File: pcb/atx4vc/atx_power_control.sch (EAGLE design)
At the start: 60 parts, among them IC2 REG1117, IC3 STM32F042F4, IC4 MY_7905DT, J1 ATX24RH, SW1 324_SW, SW2 324_SW, SW3 324_SW, SW4 324_SW, SW5 324_SW, SW6 324_SW, SW7 324_SW, U1 USBC_16P, U2 USBC_16P

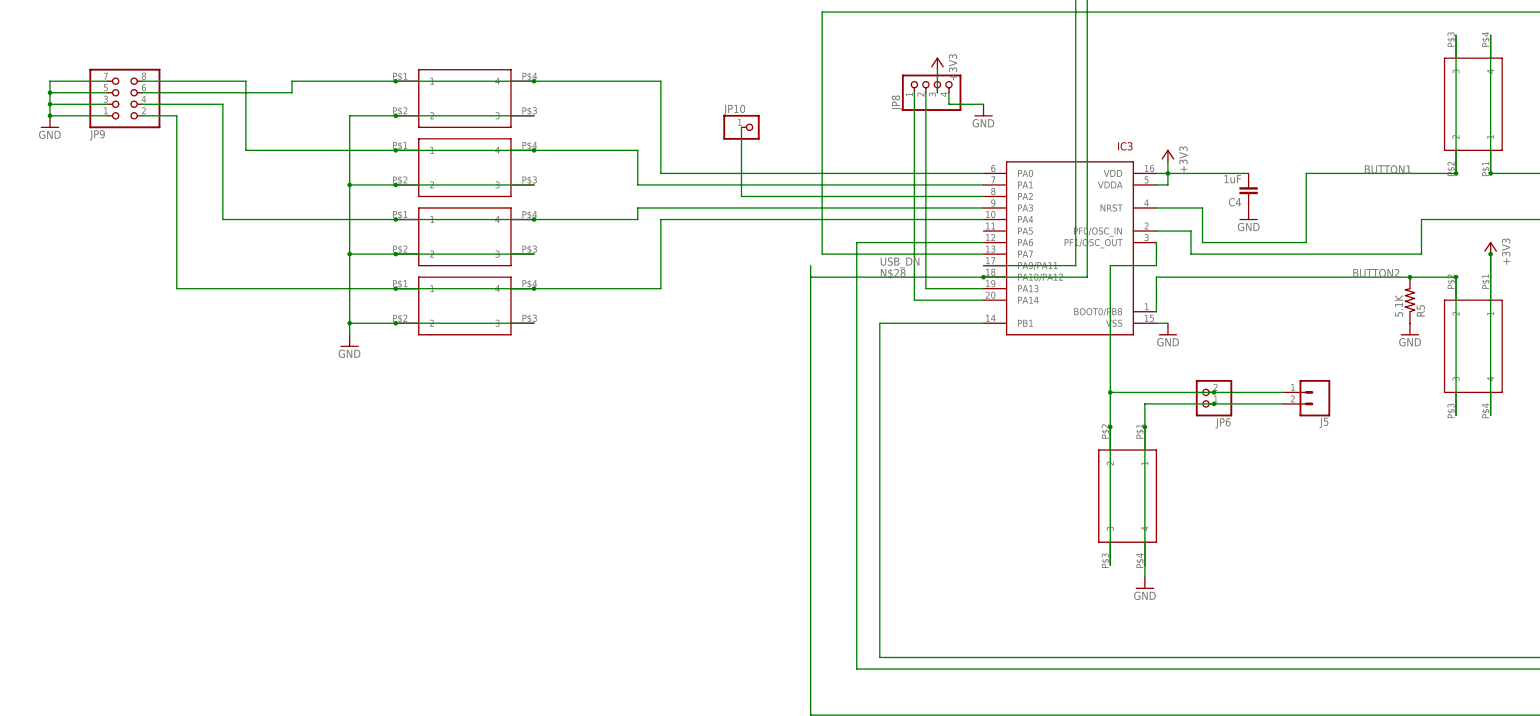
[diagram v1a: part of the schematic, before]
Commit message: added UART RX header, brightness button shared with DFU button
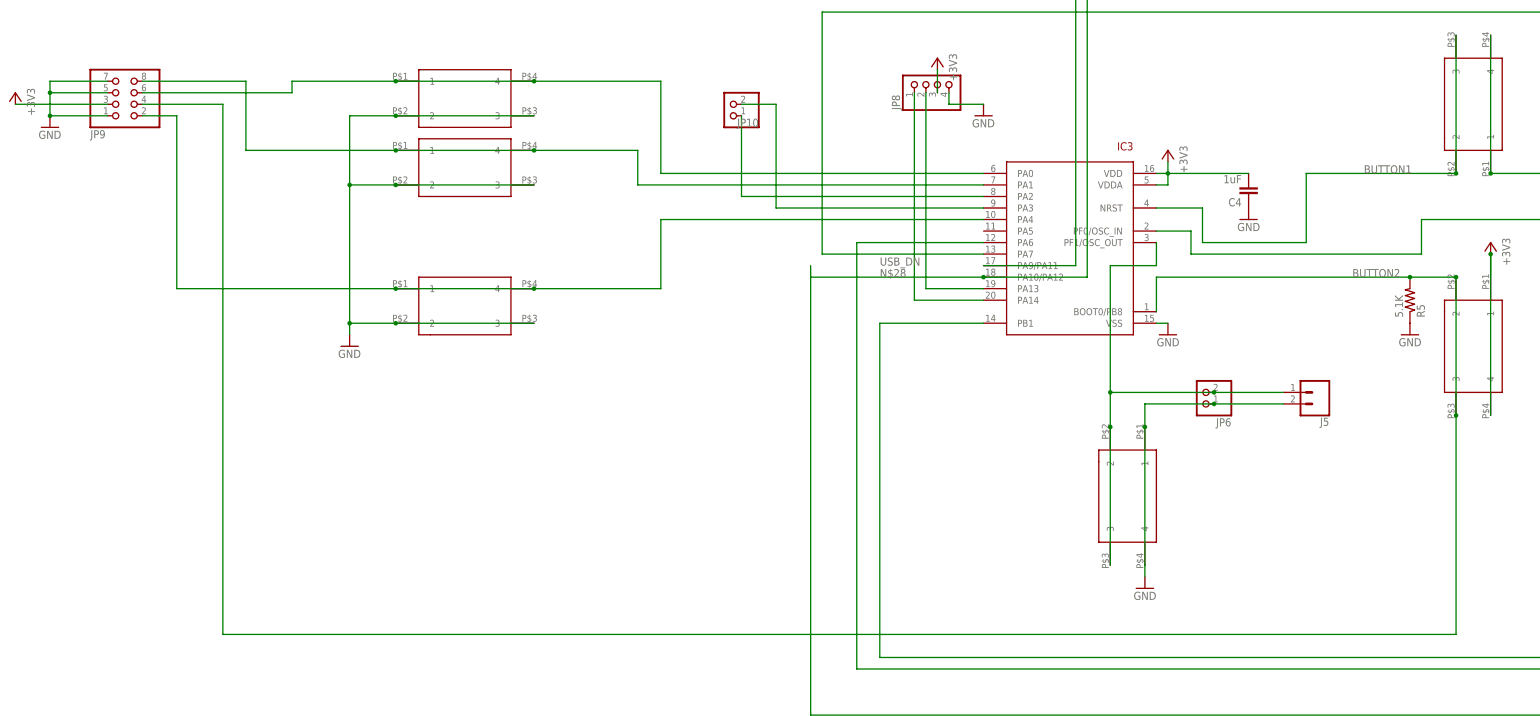
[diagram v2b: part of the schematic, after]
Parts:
- removed SW6: 324_SW, 3pos_slide_switch_centered:324_SW
- JP10: device adafruit_changed:PINHD-1X1 -> pinhead:PINHD-1X2
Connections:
- removed net N$30: IC3.PA3, JP9.4, SW6.1, SW6.4
- new net N$12: IC3.PA3, JP10.2
- net +3V3: now also JP9.3
- net BUTTON2: now also JP9.4
- net GND: no longer JP9.3, SW6.2, SW6.3
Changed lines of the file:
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@@
 <part name="J8" library="atx_power_control" deviceset="CONN_02" device="3.5MM"/>
 <part name="SW5" library="3pos_slide_switch_centered" deviceset="324_SW" device="" value="324_SW"/>
-<part name="SW6" library="3pos_slide_switch_centered" deviceset="324_SW" device="" value="324_SW"/>
 <part name="SW7" library="3pos_slide_switch_centered" deviceset="324_SW" device="" value="324_SW"/>
 <part name="GND30" library="backplane" deviceset="GND" device=""/>
 <part name="JP9" library="pinhead" library_urn="urn:adsk.eagle:library:325" deviceset="PINHD-2X4" device="" package3d_urn="urn:adsk.eagle:package:22461/2"/>
-<part name="JP10" library="adafruit_changed" deviceset="PINHD-1X1" device=""/>
+<part name="JP10" library="pinhead" library_urn="urn:adsk.eagle:library:325" deviceset="PINHD-1X2" device="" package3d_urn="urn:adsk.eagle:package:22435/2"/>
 <part name="U1" library="my_usbc_16p" deviceset="USBC_16P" device=""/>
 <part name="GND31" library="supply1" deviceset="GND" device=""/>
 <part name="R12" library="joyAnalog" deviceset="RESISTOR" device="0805-RES" value="5.1K"/>
 <part name="R13" library="joyAnalog" deviceset="RESISTOR" device="0805-RES" value="5.1K"/>
+<part name="+3V3" library="supply1" library_urn="urn:adsk.eagle:library:371" deviceset="+3V3" device=""/>
 </parts>
 <sheets>
@@
 </instance>
 <instance part="SW5" gate="G$1" x="-132.08" y="43.18" smashed="yes" rot="MR180"/>
-<instance part="SW6" gate="G$1" x="-132.08" y="27.94" smashed="yes" rot="MR180"/>
 <instance part="SW7" gate="G$1" x="-132.08" y="12.7" smashed="yes" rot="MR180"/>
 <instance part="GND30" gate="1" x="-223.52" y="50.8" smashed="yes">
@@
 <attribute name="VALUE" x="-214.63" y="66.04" size="1.778" layer="96" rot="MR180"/>
 </instance>
-<instance part="JP10" gate="G$1" x="-68.58" y="50.8" smashed="yes">
-<attribute name="NAME" x="-74.93" y="53.975" size="1.778" layer="95"/>
-<attribute name="VALUE" x="-74.93" y="45.72" size="1.778" layer="96"/>
+<instance part="JP10" gate="G$1" x="-73.66" y="55.88" smashed="yes" rot="R180">
+<attribute name="NAME" x="-67.31" y="52.705" size="1.778" layer="95" rot="R180"/>
+<attribute name="VALUE" x="-67.31" y="60.96" size="1.778" layer="96" rot="R180"/>
 </instance>
 <instance part="U1" gate="G$1" x="279.4" y="111.76" smashed="yes" rot="MR0"/>
@@
 <attribute name="NAME" x="250.19" y="128.4986" size="1.778" layer="95" rot="MR0"/>
 <attribute name="VALUE" x="250.19" y="123.698" size="1.778" layer="96" rot="MR0"/>
+</instance>
+<instance part="+3V3" gate="G$1" x="-231.14" y="58.42" smashed="yes" rot="MR0">
+<attribute name="VALUE" x="-228.6" y="53.34" size="1.778" layer="96" rot="MR90"/>
 </instance>
 </instances>
@@
 <pinref part="SW5" gate="G$1" pin="3"/>
 <pinref part="SW5" gate="G$1" pin="2"/>
-<wire x1="-157.48" y1="38.1" x2="-157.48" y2="22.86" width="0.1524" layer="91"/>
-<wire x1="-157.48" y1="22.86" x2="-157.48" y2="7.62" width="0.1524" layer="91"/>
+<wire x1="-157.48" y1="38.1" x2="-157.48" y2="7.62" width="0.1524" layer="91"/>
 <wire x1="-157.48" y1="7.62" x2="-157.48" y2="5.08" width="0.1524" layer="91"/>
 <wire x1="-116.84" y1="38.1" x2="-147.32" y2="38.1" width="0.1524" layer="91"/>
@@
 <junction x="-147.32" y="38.1"/>
 <junction x="-157.48" y="38.1"/>
-<pinref part="SW6" gate="G$1" pin="3"/>
-<pinref part="SW6" gate="G$1" pin="2"/>
-<wire x1="-116.84" y1="22.86" x2="-147.32" y2="22.86" width="0.1524" layer="91"/>
-<wire x1="-147.32" y1="22.86" x2="-157.48" y2="22.86" width="0.1524" layer="91"/>
-<junction x="-147.32" y="22.86"/>
-<junction x="-157.48" y="22.86"/>
 <pinref part="SW7" gate="G$1" pin="3"/>
 <pinref part="SW7" gate="G$1" pin="2"/>
@@
 <wire x1="-210.82" y1="60.96" x2="-223.52" y2="60.96" width="0.1524" layer="91"/>
 <wire x1="-223.52" y1="60.96" x2="-223.52" y2="58.42" width="0.1524" layer="91"/>
-<wire x1="-223.52" y1="58.42" x2="-223.52" y2="55.88" width="0.1524" layer="91"/>
-<wire x1="-223.52" y1="55.88" x2="-223.52" y2="53.34" width="0.1524" layer="91"/>
+<wire x1="-223.52" y1="58.42" x2="-223.52" y2="53.34" width="0.1524" layer="91"/>
 <wire x1="-210.82" y1="58.42" x2="-223.52" y2="58.42" width="0.1524" layer="91"/>
 <junction x="-223.52" y="58.42"/>
-<wire x1="-210.82" y1="55.88" x2="-223.52" y2="55.88" width="0.1524" layer="91"/>
-<junction x="-223.52" y="55.88"/>
 <wire x1="-210.82" y1="53.34" x2="-223.52" y2="53.34" width="0.1524" layer="91"/>
 <junction x="-223.52" y="53.34"/>
 <pinref part="JP9" gate="A" pin="1"/>
-<pinref part="JP9" gate="A" pin="3"/>
 <pinref part="JP9" gate="A" pin="5"/>
 <pinref part="JP9" gate="A" pin="7"/>
@@
 <wire x1="-27.94" y1="63.5" x2="-27.94" y2="58.42" width="0.1524" layer="91"/>
 <pinref part="JP8" gate="A" pin="3"/>
+</segment>
+<segment>
+<pinref part="JP9" gate="A" pin="3"/>
+<pinref part="+3V3" gate="G$1" pin="+3V3"/>
+<wire x1="-210.82" y1="55.88" x2="-231.14" y2="55.88" width="0.1524" layer="91"/>
 </segment>
 </net>
@@
 <wire x1="76.2" y1="17.78" x2="86.36" y2="17.78" width="0.1524" layer="91"/>
 <junction x="76.2" y="17.78"/>
+<wire x1="86.36" y1="-12.7" x2="86.36" y2="-60.96" width="0.1524" layer="91"/>
+<wire x1="86.36" y1="-60.96" x2="-185.42" y2="-60.96" width="0.1524" layer="91"/>
+<junction x="86.36" y="-12.7"/>
+<wire x1="-185.42" y1="55.88" x2="-203.2" y2="55.88" width="0.1524" layer="91"/>
+<pinref part="JP9" gate="A" pin="4"/>
+<wire x1="-185.42" y1="-60.96" x2="-185.42" y2="55.88" width="0.1524" layer="91"/>
 </segment>
 </net>
@@
 </segment>
 </net>
-<net name="N$30" class="0">
-<segment>
-<pinref part="IC3" gate="G$1" pin="PA3"/>
-<wire x1="-17.78" y1="33.02" x2="-93.98" y2="33.02" width="0.1524" layer="91"/>
-<pinref part="SW6" gate="G$1" pin="4"/>
-<wire x1="-93.98" y1="30.48" x2="-116.84" y2="30.48" width="0.1524" layer="91"/>
-<wire x1="-93.98" y1="33.02" x2="-93.98" y2="30.48" width="0.1524" layer="91"/>
-<pinref part="SW6" gate="G$1" pin="1"/>
-<wire x1="-116.84" y1="30.48" x2="-147.32" y2="30.48" width="0.1524" layer="91"/>
-<junction x="-116.84" y="30.48"/>
-<wire x1="-147.32" y1="30.48" x2="-185.42" y2="30.48" width="0.1524" layer="91"/>
-<wire x1="-185.42" y1="30.48" x2="-185.42" y2="55.88" width="0.1524" layer="91"/>
-<junction x="-147.32" y="30.48"/>
-<wire x1="-185.42" y1="55.88" x2="-203.2" y2="55.88" width="0.1524" layer="91"/>
-<pinref part="JP9" gate="A" pin="4"/>
-</segment>
-</net>
 <net name="N$13" class="0">
 <segment>
@@
 <pinref part="IC3" gate="G$1" pin="PA2"/>
 <wire x1="-17.78" y1="35.56" x2="-71.12" y2="35.56" width="0.1524" layer="91"/>
-<wire x1="-71.12" y1="35.56" x2="-71.12" y2="50.8" width="0.1524" layer="91"/>
+<wire x1="-71.12" y1="35.56" x2="-71.12" y2="53.34" width="0.1524" layer="91"/>
 <pinref part="JP10" gate="G$1" pin="1"/>
 </segment>
@@
 </segment>
 </net>
+<net name="N$12" class="0">
+<segment>
+<pinref part="IC3" gate="G$1" pin="PA3"/>
+<wire x1="-17.78" y1="33.02" x2="-63.5" y2="33.02" width="0.1524" layer="91"/>
+<wire x1="-63.5" y1="33.02" x2="-63.5" y2="55.88" width="0.1524" layer="91"/>
+<pinref part="JP10" gate="G$1" pin="2"/>
+<wire x1="-63.5" y1="55.88" x2="-71.12" y2="55.88" width="0.1524" layer="91"/>
+</segment>
+</net>
